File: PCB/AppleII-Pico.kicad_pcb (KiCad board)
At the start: 2 copper layers, 106.3 x 56.7 mm, 31 parts, among them J1 Apple II, J2 DB15_Female_HighDensity_Mount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, J3 NOPAL, J4 Conn_02x08_Odd_Even, J5 Conn_02x08_Odd_Even, SW1 Pico Reset, U1 74LCX16245, U2 74LCX16245, U5 PALCE16V8H, U6 Pi PICO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

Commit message: tweaks before sending to JLCPCB
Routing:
- net GND: track 208.1 -> 216.9 mm, vias 25 -> 27
- net nDATADIR: track 63.8 -> 65.6 mm
- net nIOSEL: track 64.5 -> 63.4 mm
- net D3: track 12.5 -> 13.4 mm
- net D0: track 18.8 -> 17.9 mm
- net D1: track 16.6 -> 15.9 mm
- net nMSBOE: track 42.8 -> 42.1 mm
- net nLSBOE: track 63.3 -> 62.6 mm
- net A0: track 22.9 -> 22.2 mm
- net nDATAOE: track 69.7 -> 69.0 mm

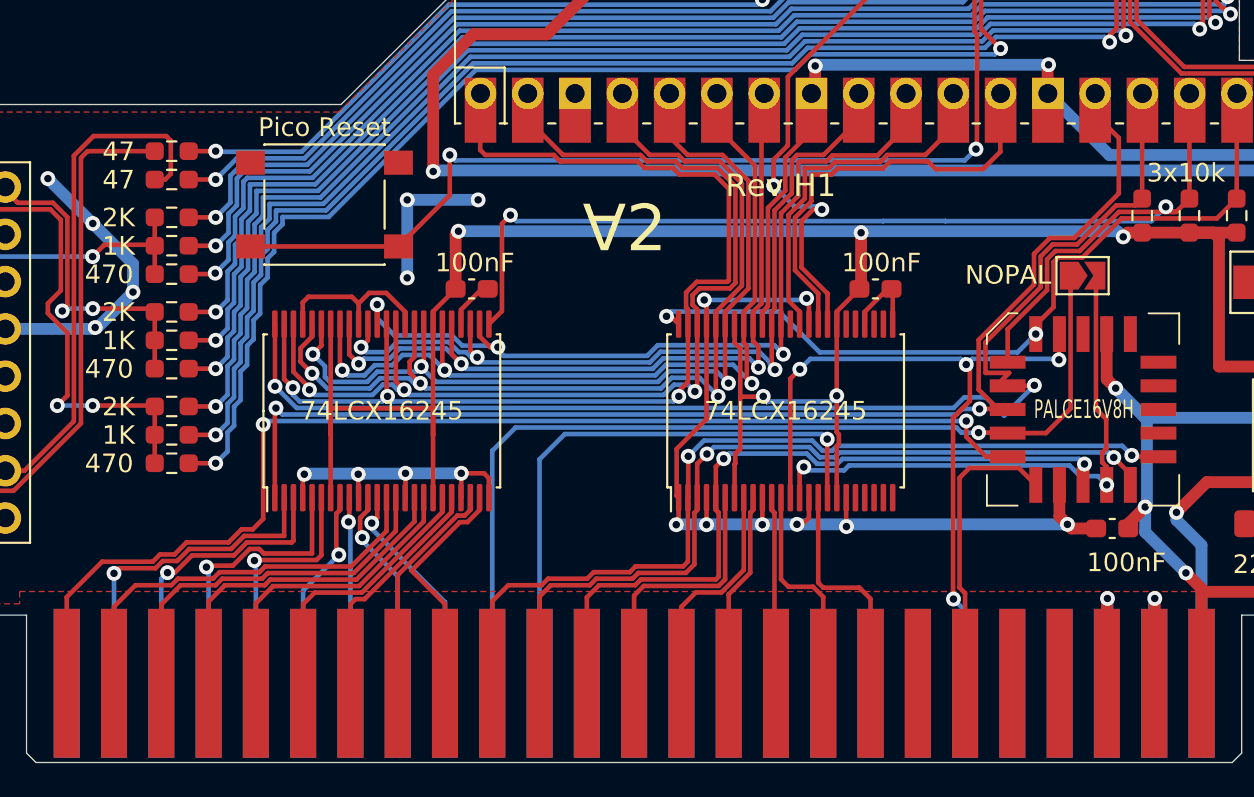
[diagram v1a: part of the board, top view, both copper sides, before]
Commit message: Fix TSSOP-48 footprint and move NOPAL
 - Use correct footprint for the TSSOP-48 case (closes #2)
 - Rename NOPAL to NOGAL and move it into the GAL footprint (closes #3)
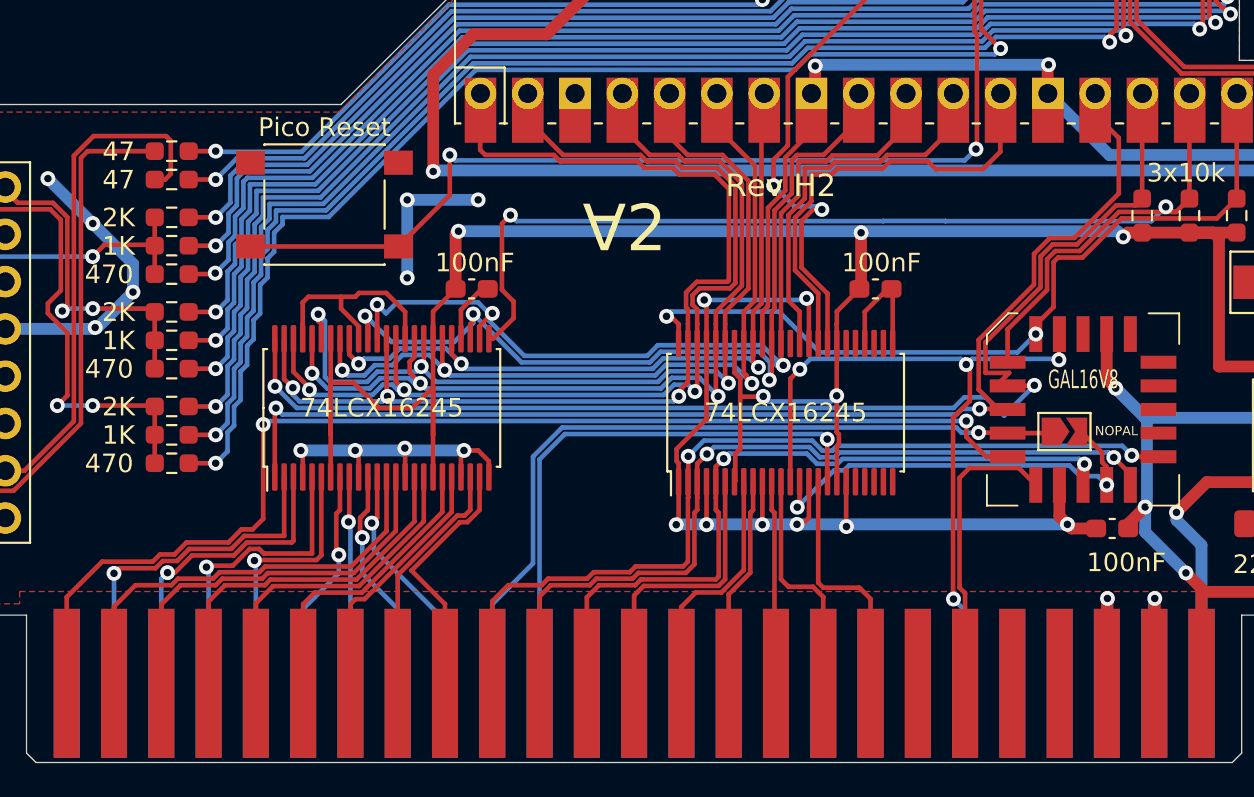
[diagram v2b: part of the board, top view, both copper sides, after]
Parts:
- U1, U2: footprint Package_SO:TSSOP-48_8x12.5mm_P0.5mm -> Package_SO:TSSOP-48_6.1x12.5mm_P0.5mm
- U5: value PALCE16V8H -> GAL16V8
- moved J3 8.43 mm to (165.2, 116.7)
- moved U1 0.16 mm to (128.6, 115.4)
- moved U2 0.09 mm to (150.3, 115.7)
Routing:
- net GND: track 216.9 -> 229.1 mm
- net nDEVSEL: track 51.9 -> 41.7 mm
- net nCARDSEL: track 30.3 -> 23.6 mm
- net +3V3: track 128.3 -> 126.1 mm
- net LD2: track 50.4 -> 48.3 mm
- net LD6: track 43.7 -> 45.5 mm
- net LD7: track 44.8 -> 46.5 mm
- net LD4: track 44.5 -> 42.9 mm
- net LD5: track 41.4 -> 39.8 mm
- net LD1: track 55.3 -> 53.7 mm
- net LD0: track 58.6 -> 57.0 mm
- net nLSBOE: track 62.6 -> 64.1 mm
- net D6: track 11.0 -> 12.1 mm
- net D4: track 10.9 -> 12.0 mm
- net D0: track 17.9 -> 19.0 mm
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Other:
- board text added: "Rev H2"
- board text removed: "Rev H1"

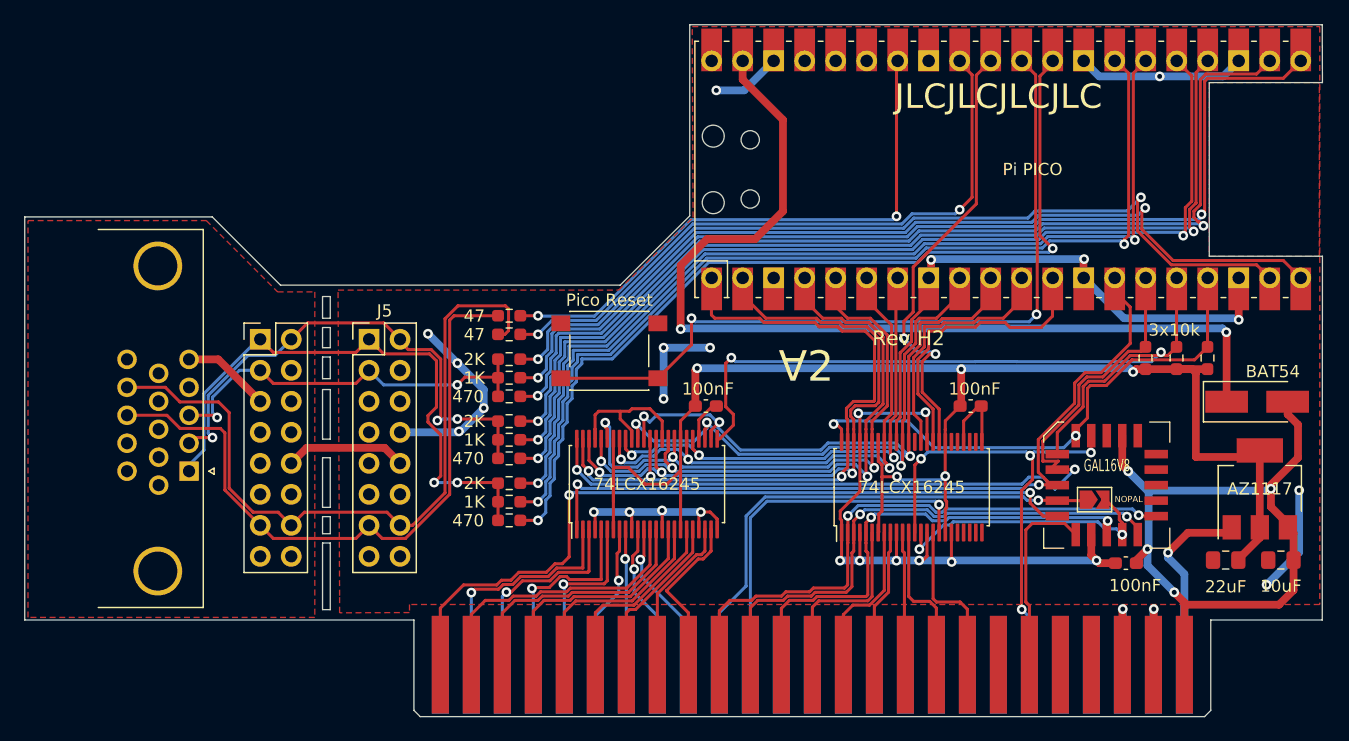
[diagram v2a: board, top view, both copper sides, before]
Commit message: silkscreen tweaks
closes #4
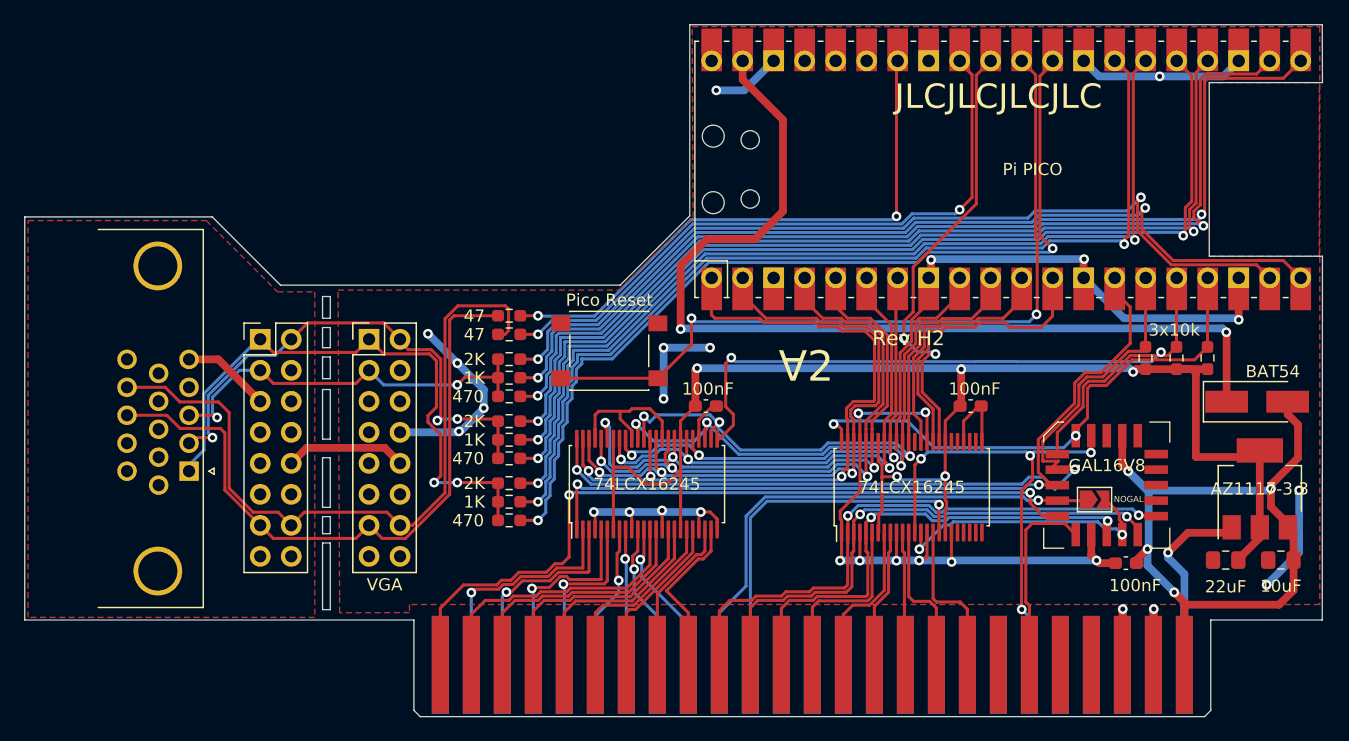
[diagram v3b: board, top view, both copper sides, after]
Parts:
- J3: value NOPAL -> NOGAL
- J4, J5: value Conn_02x08_Odd_Even -> VGA
- U7: value AZ1117 -> AZ1117-3.3
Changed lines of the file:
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@@
     )
     (fp_text value "GAL16V8" (at 0.016 -1.608) (layer "F.SilkS")
-      (effects (font (size 1 0.6) (thickness 0.15)))
+      (effects (font (size 1 1) (thickness 0.15)))
     )
     (fp_text user "${REFERENCE}" (at 0 0) (layer "F.Fab")
@@
       (effects (font (size 1 1) (thickness 0.15)))
     )
-    (fp_text value "AZ1117" (at 0 0 180) (layer "F.SilkS")
+    (fp_text value "AZ1117-3.3" (at 0 0 180) (layer "F.SilkS")
       (effects (font (size 1 1) (thickness 0.15)))
     )
@@
       (effects (font (size 1 1) (thickness 0.15)))
     )
-    (fp_text value "NOPAL" (at 2.794 -0.0332) (layer "F.SilkS")
+    (fp_text value "NOGAL" (at 2.794 -0.0332) (layer "F.SilkS")
       (effects (font (size 0.5 0.5) (thickness 0.1)))
     )
@@
     (property "Sheetname" "")
     (attr through_hole)
-    (fp_text reference "J5" (at 1.27 -2.33) (layer "F.SilkS")
-      (effects (font (size 1 1) (thickness 0.15)))
-    )
-    (fp_text value "Conn_02x08_Odd_Even" (at 1.27 20.11) (layer "F.Fab")
+    (fp_text reference "J5" (at 1.27 -2.33) (layer "F.Fab")
+      (effects (font (size 1 1) (thickness 0.15)))
+    )
+    (fp_text value "VGA" (at 1.27 20.11) (layer "F.SilkS")
       (effects (font (size 1 1) (thickness 0.15)))
     )
@@
       (effects (font (size 1 1) (thickness 0.15)))
     )
-    (fp_text value "Conn_02x08_Odd_Even" (at 1.27 20.11) (layer "F.Fab")
-      (effects (font (size 1 1) (thickness 0.15)))
-    )
+    (fp_text value "VGA" (at 1.27 20.11) (layer "F.Fab")
+      (effects (font (size 1 1) (thickness 0.15)))
+    )

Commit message: Version h2 sent to JLCPCB for production
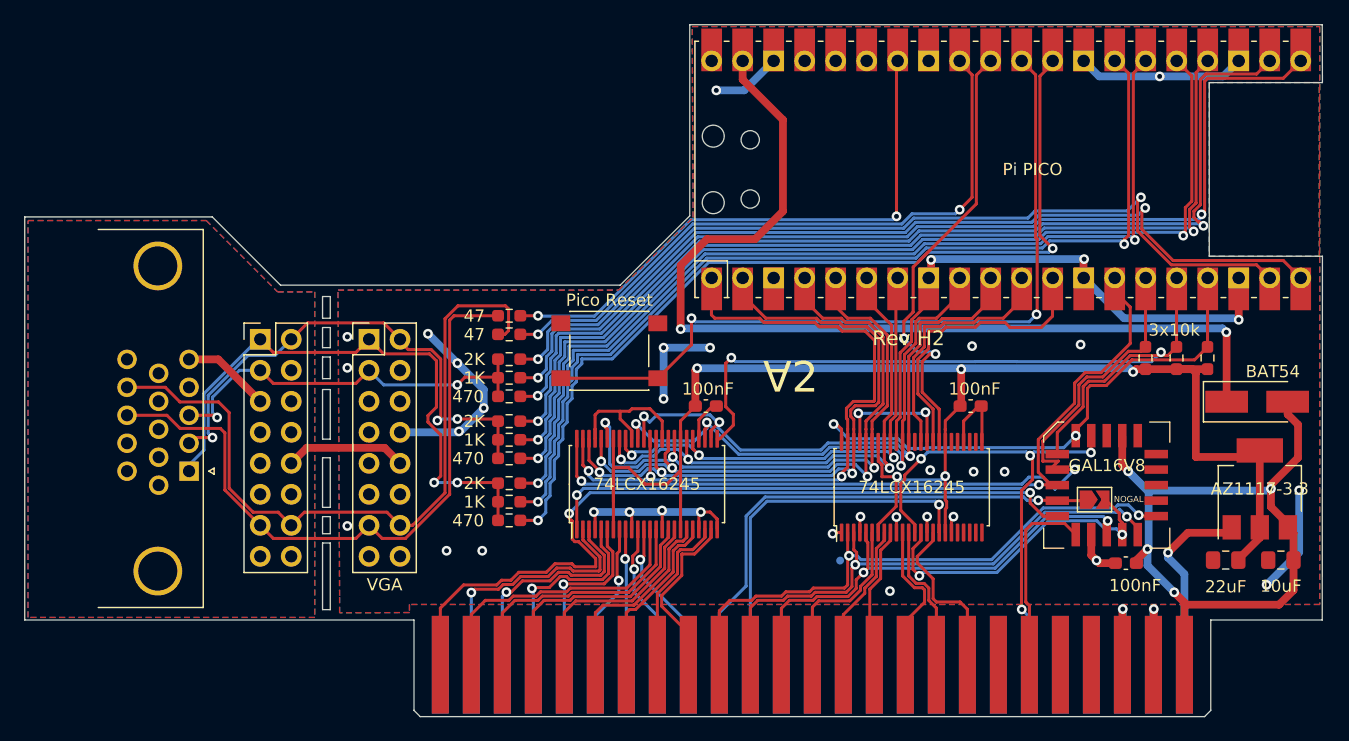
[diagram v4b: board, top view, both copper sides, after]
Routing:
- net GND: track 229.1 -> 194.0 mm, vias 27 -> 38
- net nCARDSEL: track 23.6 -> 27.2 mm
- net nIOSEL: track 63.4 -> 66.4 mm
- net D0: track 19.0 -> 21.3 mm
- net D1: track 17.0 -> 19.0 mm
- net A14: track 10.9 -> 12.6 mm
- net nWR: track 13.1 -> 14.2 mm
- net nSYSRESET: track 40.2 -> 41.2 mm
- net A11: track 15.2 -> 14.3 mm
- net A12: track 13.0 -> 12.2 mm
- net nDATADIR: track 64.5 -> 63.8 mm
- net A7: track 13.6 -> 14.3 mm
- net D2: track 16.6 -> 17.1 mm
- added copper zone on B.Cu, net GND
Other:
- board text removed: "JLCJLCJLCJLC"
